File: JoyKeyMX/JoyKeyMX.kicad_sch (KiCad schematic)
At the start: 31 parts, among them J1 DB9_Female, J2 Conn_01x16, J3 Conn_01x02, SW1 SW_WITHLED, SW2 SW_WITHLED, SW4 SW_WITHLED, SW5 SW_WITHLED, SW6 SW_WITHLED, SW7 SW_WITHLED

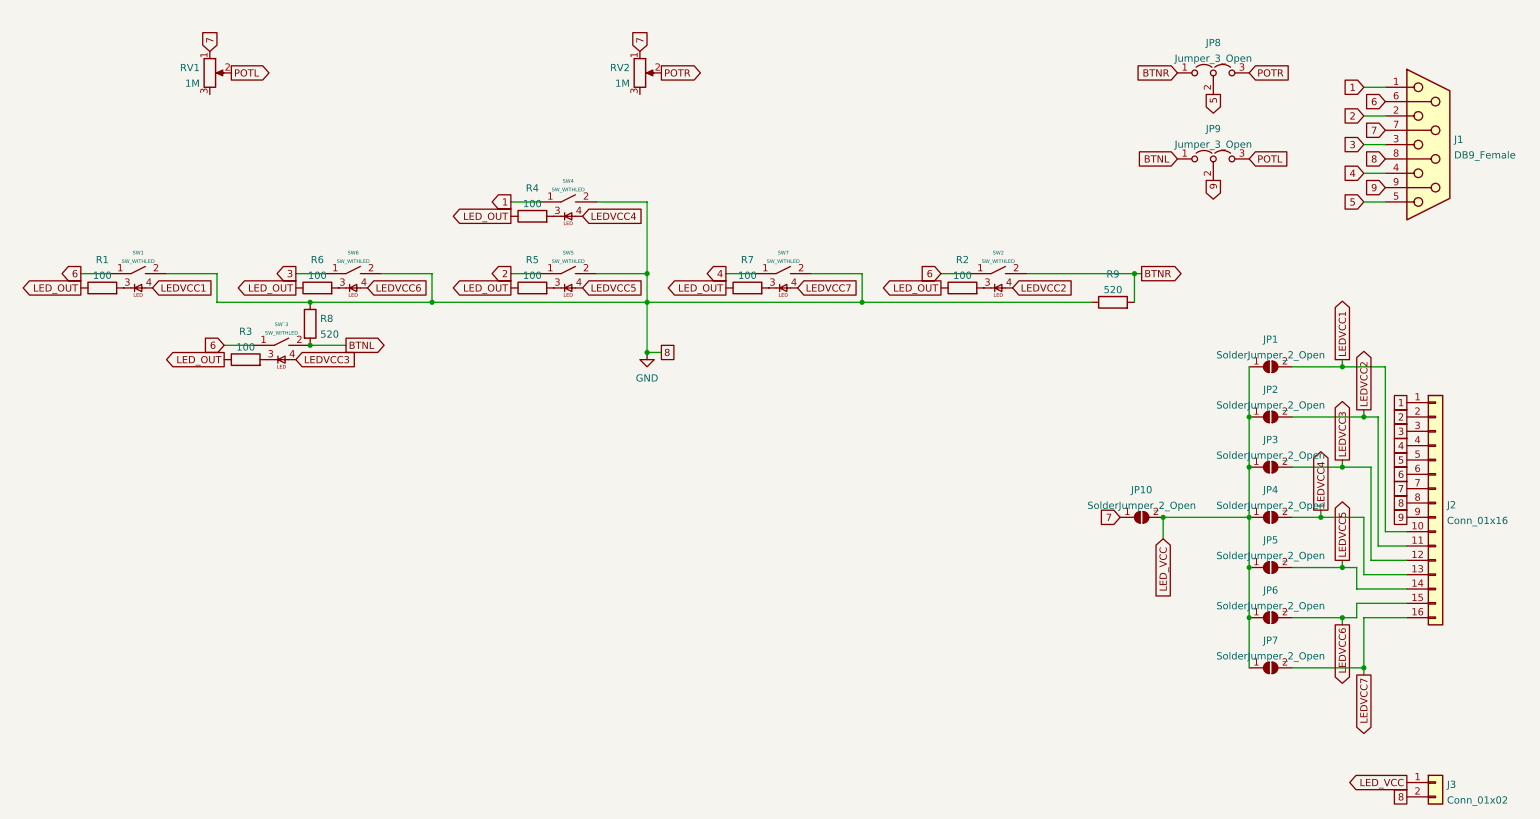
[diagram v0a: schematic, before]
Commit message: Add pins for pots on header
Add branding, fit and finish
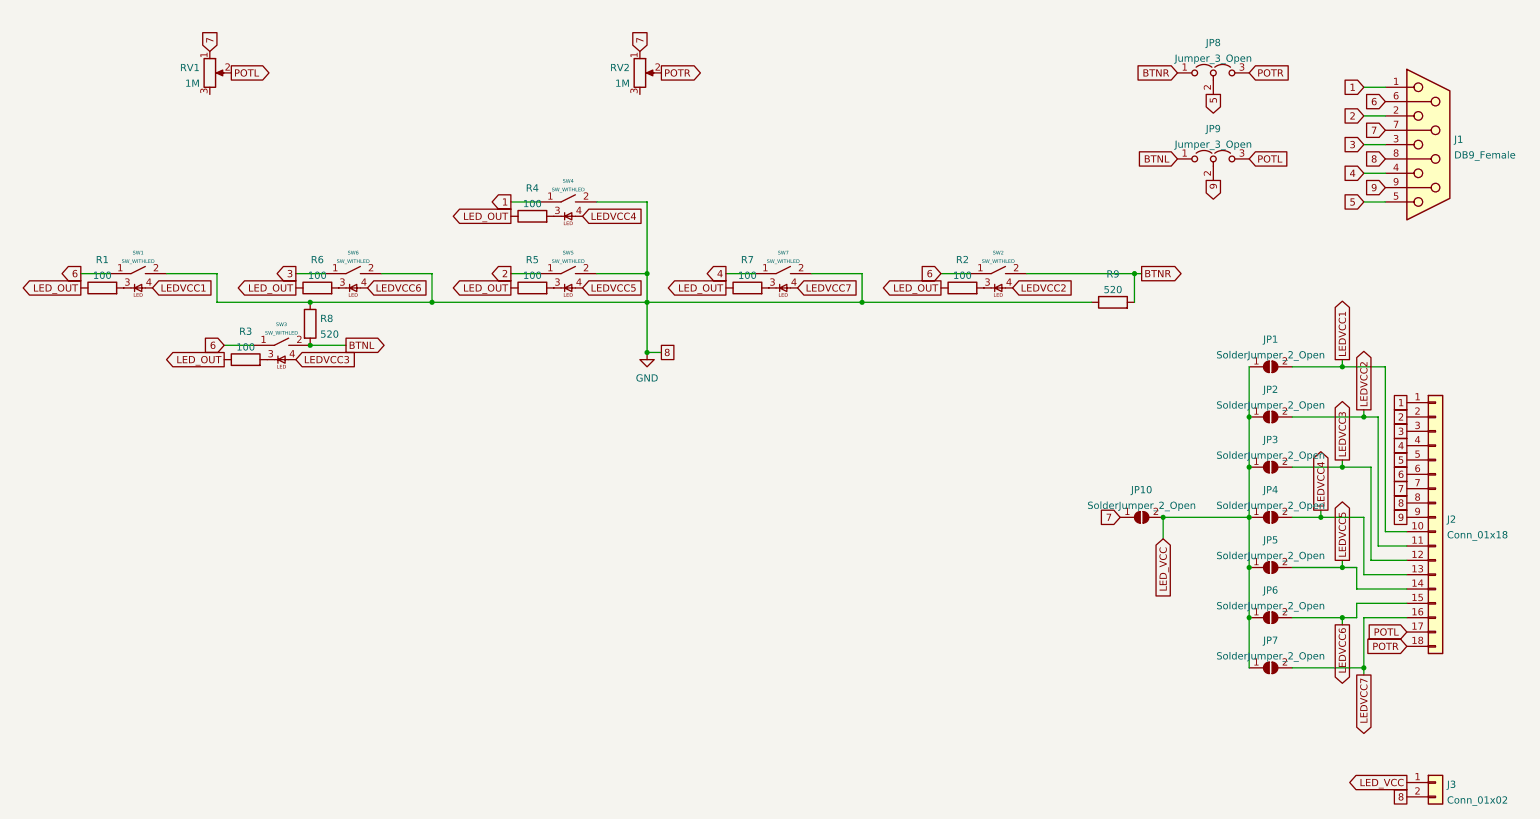
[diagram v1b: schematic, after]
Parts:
- J2: value Conn_01x16 -> Conn_01x18; footprint Connector_PinHeader_2.54mm:PinHeader_1x16_P2.54mm_Vertical -> Connector_PinHeader_2.54mm:PinHeader_1x18_P2.54mm_Vertical; symbol Connector_Generic:Conn_01x16 -> Connector_Generic:Conn_01x18
- renumbered SW`3 to SW3
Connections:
- net POTL: now also J2.17 (Pin_17)
- net POTR: now also J2.18 (Pin_18)
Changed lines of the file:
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@@
     (stroke (width 0) (type default) (color 0 0 0 0))
   )
-  (wire (pts (xy 262.89 109.22) (xy 257.81 109.22))
-    (stroke (width 0) (type default) (color 0 0 0 0))
-  )
-  (wire (pts (xy 262.89 114.3) (xy 255.27 114.3))
+  (wire (pts (xy 255.27 121.92) (xy 262.89 121.92))
     (stroke (width 0) (type default) (color 0 0 0 0))
   )
@@
     (stroke (width 0) (type default) (color 0 0 0 0))
   )
-  (wire (pts (xy 262.89 111.76) (xy 256.54 111.76))
-    (stroke (width 0) (type default) (color 0 0 0 0))
-  )
   (wire (pts (xy 255.27 33.02) (xy 259.08 33.02))
     (stroke (width 0) (type default) (color 0 0 0 0))
@@
     (stroke (width 0) (type default) (color 0 0 0 0))
   )
-  (wire (pts (xy 262.89 116.84) (xy 254 116.84))
-    (stroke (width 0) (type default) (color 0 0 0 0))
-  )
   (wire (pts (xy 142.24 60.96) (xy 147.32 60.96))
     (stroke (width 0) (type default) (color 0 0 0 0))
@@
     (stroke (width 0) (type default) (color 0 0 0 0))
   )
+  (wire (pts (xy 259.08 106.68) (xy 262.89 106.68))
+    (stroke (width 0) (type default) (color 0 0 0 0))
+  )
   (wire (pts (xy 104.14 60.96) (xy 109.22 60.96))
     (stroke (width 0) (type default) (color 0 0 0 0))
@@
     (stroke (width 0) (type default) (color 0 0 0 0))
   )
+  (wire (pts (xy 254 116.84) (xy 262.89 116.84))
+    (stroke (width 0) (type default) (color 0 0 0 0))
+  )
   (wire (pts (xy 215.9 60.96) (xy 214.63 60.96))
     (stroke (width 0) (type default) (color 0 0 0 0))
@@
     (stroke (width 0) (type default) (color 0 0 0 0))
   )
-  (wire (pts (xy 262.89 119.38) (xy 254 119.38))
+  (wire (pts (xy 257.81 109.22) (xy 262.89 109.22))
     (stroke (width 0) (type default) (color 0 0 0 0))
   )
@@
     (stroke (width 0) (type default) (color 0 0 0 0))
   )
+  (wire (pts (xy 256.54 111.76) (xy 262.89 111.76))
+    (stroke (width 0) (type default) (color 0 0 0 0))
+  )
   (wire (pts (xy 255.27 104.14) (xy 247.65 104.14))
     (stroke (width 0) (type default) (color 0 0 0 0))
   )
+  (wire (pts (xy 255.27 130.81) (xy 255.27 121.92))
+    (stroke (width 0) (type default) (color 0 0 0 0))
+  )
   (wire (pts (xy 214.63 60.96) (xy 195.58 60.96))
     (stroke (width 0) (type default) (color 0 0 0 0))
@@
     (stroke (width 0) (type default) (color 0 0 0 0))
   )
-  (wire (pts (xy 262.89 121.92) (xy 255.27 121.92))
+  (wire (pts (xy 255.27 114.3) (xy 262.89 114.3))
     (stroke (width 0) (type default) (color 0 0 0 0))
   )
@@
     (stroke (width 0) (type default) (color 0 0 0 0))
   )
+  (wire (pts (xy 254 119.38) (xy 262.89 119.38))
+    (stroke (width 0) (type default) (color 0 0 0 0))
+  )
   (wire (pts (xy 255.27 130.81) (xy 242.57 130.81))
     (stroke (width 0) (type default) (color 0 0 0 0))
@@
     (stroke (width 0) (type default) (color 0 0 0 0))
   )
-  (wire (pts (xy 262.89 106.68) (xy 259.08 106.68))
-    (stroke (width 0) (type default) (color 0 0 0 0))
-  )
   (wire (pts (xy 247.65 104.14) (xy 242.57 104.14))
     (stroke (width 0) (type default) (color 0 0 0 0))
@@
     (stroke (width 0) (type default) (color 0 0 0 0))
   )
-  (wire (pts (xy 255.27 121.92) (xy 255.27 130.81))
-    (stroke (width 0) (type default) (color 0 0 0 0))
-  )
   (wire (pts (xy 104.14 48.26) (xy 109.22 48.26))
     (stroke (width 0) (type default) (color 0 0 0 0))
@@
     )
   )
+  (global_label "POTL" (shape input) (at 262.89 124.46 180) (fields_autoplaced)
+    (effects (font (size 1.27 1.27)) (justify right))
+    (property "Intersheet References" "${INTERSHEET_REFS}" (id 0) (at 255.8807 124.3806 0)
+      (effects (font (size 1.27 1.27)) (justify right) hide)
+    )
+  )
   (global_label "LEDVCC7" (shape output) (at 255.27 132.08 270) (fields_autoplaced)
     (effects (font (size 1.27 1.27)) (justify right))
@@
     (property "Intersheet References" "${INTERSHEET_REFS}" (id 0) (at 61.6193 25.3206 0)
       (effects (font (size 1.27 1.27)) (justify left) hide)
+    )
+  )
+  (global_label "POTR" (shape input) (at 262.89 127 180) (fields_autoplaced)
+    (effects (font (size 1.27 1.27)) (justify right))
+    (property "Intersheet References" "${INTERSHEET_REFS}" (id 0) (at 255.6388 126.9206 0)
+      (effects (font (size 1.27 1.27)) (justify right) hide)
     )
   )
@@
   (symbol (lib_id "UniversalSwitchWithLED:SW_WITHLED") (at 63.5 73.66 0) (unit 1)
     (in_bom yes) (on_board yes) (fields_autoplaced)
-    (property "Reference" "SW`3" (id 0) (at 63.5 69.9622 0)
+    (property "Reference" "SW3" (id 0) (at 63.5 69.9622 0)
       (effects (font (size 0.635 0.635)))
     )
@@
     (pin "3")
   )
-  (symbol (lib_id "Connector_Generic:Conn_01x16") (at 267.97 101.6 0) (unit 1)
-    (in_bom yes) (on_board yes) (fields_autoplaced)
-    (property "Reference" "J2" (id 0) (at 270.002 101.9615 0)
+  (symbol (lib_id "Connector_Generic:Conn_01x18") (at 267.97 104.14 0) (unit 1)
+    (in_bom yes) (on_board yes) (fields_autoplaced)
+    (property "Reference" "J2" (id 0) (at 270.002 104.5015 0)
       (effects (font (size 1.27 1.27)) (justify left))
     )
-    (property "Value" "Conn_01x16" (id 1) (at 270.002 104.7366 0)
+    (property "Value" "Conn_01x18" (id 1) (at 270.002 107.2766 0)
       (effects (font (size 1.27 1.27)) (justify left))
     )
-    (property "Footprint" "Connector_PinHeader_2.54mm:PinHeader_1x16_P2.54mm_Vertical" (id 2) (at 267.97 101.6 0)
-      (effects (font (size 1.27 1.27)) hide)
-    )
-    (property "Datasheet" "~" (id 3) (at 267.97 101.6 0)
+    (property "Footprint" "Connector_PinHeader_2.54mm:PinHeader_1x18_P2.54mm_Vertical" (id 2) (at 267.97 104.14 0)
+      (effects (font (size 1.27 1.27)) hide)
+    )
+    (property "Datasheet" "~" (id 3) (at 267.97 104.14 0)
       (effects (font (size 1.27 1.27)) hide)
     )
@@
     (pin "15")
     (pin "16")
+    (pin "17")
+    (pin "18")
     (pin "2")
     (pin "3")
@@
     )
     (path "/fe557b0f-d638-42ed-8021-71dd98a76443"
-      (reference "J2") (unit 1) (value "Conn_01x16") (footprint "Connector_PinHeader_2.54mm:PinHeader_1x16_P2.54mm_Vertical")
+      (reference "J2") (unit 1) (value "Conn_01x18") (footprint "Connector_PinHeader_2.54mm:PinHeader_1x18_P2.54mm_Vertical")
     )
     (path "/e702a3ea-106a-406d-9f17-c06eda1e35d1"
@@
       (reference "SW2") (unit 1) (value "SW_WITHLED") (footprint "Universal-Switch-Footprint:MX-ALPs-PG1350-LED-FLIP")
     )
+    (path "/cb2d9bc6-1961-44c0-842e-5cc094e0af1a"
+      (reference "SW3") (unit 1) (value "SW_WITHLED") (footprint "Universal-Switch-Footprint:MX-ALPs-PG1350-LED-FLIP")
+    )
     (path "/5a768132-5548-46f5-9624-91b717ac5a4e"
       (reference "SW4") (unit 1) (value "SW_WITHLED") (footprint "Universal-Switch-Footprint:MX-ALPs-PG1350-LED-FLIP")
@@
       (reference "SW7") (unit 1) (value "SW_WITHLED") (footprint "Universal-Switch-Footprint:MX-ALPs-PG1350-LED-FLIP")
     )
-    (path "/cb2d9bc6-1961-44c0-842e-5cc094e0af1a"
-      (reference "SW`3") (unit 1) (value "SW_WITHLED") (footprint "Universal-Switch-Footprint:MX-ALPs-PG1350-LED-FLIP")
-    )
-  )
+  )

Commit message: JoyKeyMX Rev.B
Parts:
- JP1, JP2, JP3, JP4, JP5, JP6, JP7: footprint Jumper:SolderJumper-2_P1.3mm_Open_TrianglePad1.0x1.5mm -> Jumper:SolderJumper-2_P1.3mm_Bridged_RoundedPad1.0x1.5mm; symbol Jumper:SolderJumper_2_Open -> Jumper:SolderJumper_2_Bridged
- JP8, JP9: footprint Connector_PinHeader_2.54mm:PinHeader_1x03_P2.54mm_Horizontal -> Library:PinHeader_1x03_P2.54mm_Horizontal
- R1, R2, R3, R4, R5, R6, R7, R8, R9: footprint Resistor_THT:R_Axial_DIN0207_L6.3mm_D2.5mm_P7.62mm_Horizontal -> Library:R_Axial_DIN0207_L6.3mm_D2.5mm_P7.62mm_Horizontal (with value on silkscreen)
- RV1, RV2: footprint Potentiometer_THT:Potentiometer_Bourns_PTV09A-1_Single_Vertical -> Library:Potentiometer (centered)
- SW1, SW2, SW3, SW4, SW5, SW6, SW7: footprint Universal-Switch-Footprint:MX-ALPs-PG1350-LED-FLIP -> Library:MX-1U-LED
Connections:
- net LED_OUT is gone; now on net GND: R1.1, R2.1, R3.1, R4.1, R5.1, R6.1, R7.1

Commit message: JoyKey XL PCB and case revision
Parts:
- removed JP1, JP2, JP3, JP4, JP5, JP6, JP7: SolderJumper_2_Open, Jumper:SolderJumper-2_P1.3mm_Bridged_RoundedPad1.0x1.5mm, symbol Jumper:SolderJumper_2_Bridged
- removed JP10: SolderJumper_2_Open, Jumper:SolderJumper-2_P1.3mm_Open_RoundedPad1.0x1.5mm, symbol Jumper:SolderJumper_2_Open
- removed JP9: Jumper_3_Open, Library:PinHeader_1x03_P2.54mm_Horizontal, symbol Jumper:Jumper_3_Open
- added J4: Conn_01x02, Connector_PinHeader_2.54mm:PinHeader_1x02_P2.54mm_Vertical, symbol Connector_Generic:Conn_01x02
- J2: value Conn_01x18 -> Conn_01x09; footprint Connector_PinHeader_2.54mm:PinHeader_1x18_P2.54mm_Vertical -> Connector_PinHeader_2.54mm:PinHeader_1x09_P2.54mm_Vertical; symbol Connector_Generic:Conn_01x18 -> Connector_Generic:Conn_01x09
- JP1: renamed from JP8; value Jumper_3_Open -> DPDT; footprint Library:PinHeader_1x03_P2.54mm_Horizontal -> Button_Switch_THT:SW_CuK_JS202011AQN_DPDT_Angled; symbol Jumper:Jumper_3_Open -> Switch:SW_Push_DPDT
- R1, R2, R3, R4, R5, R6, R7, R8, R9: footprint Library:R_Axial_DIN0207_L6.3mm_D2.5mm_P7.62mm_Horizontal (with value on silkscreen) -> Resistor_SMD:R_0603_1608Metric
- SW1, SW2, SW3, SW4, SW5, SW6, SW7: footprint Library:MX-1U-LED -> Library:MX-1-00U-LED
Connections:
- net LED_VCC is gone; now on net 7: J3.1 (Pin_1)
- net 9: now also JP1.5 (B)
- net BTNL: now also JP1.4 (A)
- net POTL: now also JP1.6 (C), J4.1 (Pin_1); no longer J2.17 (Pin_17)
- net POTR: now also J4.2 (Pin_2); no longer J2.18 (Pin_18)
- net LEDVCC1 renamed LEDVCC
- net LEDVCC: now also SW2.4, SW3.4, SW4.4, SW5.4, SW6.4, SW7.4; no longer J2.10 (Pin_10)
- removed net LEDVCC2: J2.11 (Pin_11), SW2.4
- removed net LEDVCC3: J2.12 (Pin_12), SW3.4
- removed net LEDVCC4: J2.13 (Pin_13), SW4.4
- removed net LEDVCC5: J2.14 (Pin_14), SW5.4
- removed net LEDVCC6: J2.15 (Pin_15), SW6.4
- removed net LEDVCC7: J2.16 (Pin_16), SW7.4
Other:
- moved on the sheet: J1, J3

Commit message: Fix JoyKey XL backlight connection
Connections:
- net LEDVCC is gone; now on net 7: SW1.4, SW2.4, SW3.4, SW4.4, SW5.4, SW6.4, SW7.4
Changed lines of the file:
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@@
+    (stroke (width 0) (type default))
+  )
+  (wire (pts (xy 224.79 46.99) (xy 228.6 46.99))
     (stroke (width 0) (type default))
   )
@@
     )
   )
-  (global_label "LEDVCC" (shape input) (at 154.94 63.5 0) (fields_autoplaced)
-    (effects (font (size 1.27 1.27)) (justify left))
-    (property "Intersheetrefs" "${INTERSHEET_REFS}" (at 164.9215 63.5 0)
+  (global_label "LED_VCC" (shape input) (at 154.94 63.5 0) (fields_autoplaced)
+    (effects (font (size 1.27 1.27)) (justify left))
+    (property "Intersheetrefs" "${INTERSHEET_REFS}" (at 165.8891 63.5 0)
       (effects (font (size 1.27 1.27)) (justify left) hide)
     )
@@
     )
   )
-  (global_label "7" (shape input) (at 228.6 46.99 180) (fields_autoplaced)
-    (effects (font (size 1.27 1.27)) (justify right))
-    (property "Intersheetrefs" "${INTERSHEET_REFS}" (at 224.9774 46.9106 0)
+  (global_label "7" (shape input) (at 224.79 46.99 180) (fields_autoplaced)
+    (effects (font (size 1.27 1.27)) (justify right))
+    (property "Intersheetrefs" "${INTERSHEET_REFS}" (at 221.1674 46.9106 0)
       (effects (font (size 1.27 1.27)) (justify right) hide)
     )
@@
     )
   )
-  (global_label "LEDVCC" (shape input) (at 66.04 76.2 0) (fields_autoplaced)
-    (effects (font (size 1.27 1.27)) (justify left))
-    (property "Intersheetrefs" "${INTERSHEET_REFS}" (at 76.0215 76.2 0)
+  (global_label "LED_VCC" (shape input) (at 66.04 76.2 0) (fields_autoplaced)
+    (effects (font (size 1.27 1.27)) (justify left))
+    (property "Intersheetrefs" "${INTERSHEET_REFS}" (at 76.9891 76.2 0)
       (effects (font (size 1.27 1.27)) (justify left) hide)
     )
@@
     )
   )
-  (global_label "LEDVCC" (shape input) (at 78.74 63.5 0) (fields_autoplaced)
-    (effects (font (size 1.27 1.27)) (justify left))
-    (property "Intersheetrefs" "${INTERSHEET_REFS}" (at 88.7215 63.5 0)
+  (global_label "LED_VCC" (shape input) (at 78.74 63.5 0) (fields_autoplaced)
+    (effects (font (size 1.27 1.27)) (justify left))
+    (property "Intersheetrefs" "${INTERSHEET_REFS}" (at 89.6891 63.5 0)
       (effects (font (size 1.27 1.27)) (justify left) hide)
     )
@@
     )
   )
-  (global_label "LEDVCC" (shape input) (at 116.84 50.8 0) (fields_autoplaced)
-    (effects (font (size 1.27 1.27)) (justify left))
-    (property "Intersheetrefs" "${INTERSHEET_REFS}" (at 126.8215 50.8 0)
+  (global_label "LED_VCC" (shape input) (at 116.84 50.8 0) (fields_autoplaced)
+    (effects (font (size 1.27 1.27)) (justify left))
+    (property "Intersheetrefs" "${INTERSHEET_REFS}" (at 127.7891 50.8 0)
       (effects (font (size 1.27 1.27)) (justify left) hide)
     )
@@
     )
   )
-  (global_label "LEDVCC" (shape input) (at 116.84 63.5 0) (fields_autoplaced)
-    (effects (font (size 1.27 1.27)) (justify left))
-    (property "Intersheetrefs" "${INTERSHEET_REFS}" (at 126.8215 63.5 0)
-      (effects (font (size 1.27 1.27)) (justify left) hide)
-    )
-  )
-  (global_label "LEDVCC" (shape input) (at 193.04 63.5 0) (fields_autoplaced)
-    (effects (font (size 1.27 1.27)) (justify left))
-    (property "Intersheetrefs" "${INTERSHEET_REFS}" (at 203.0215 63.5 0)
-      (effects (font (size 1.27 1.27)) (justify left) hide)
-    )
-  )
-  (global_label "LEDVCC" (shape input) (at 40.64 63.5 0) (fields_autoplaced)
-    (effects (font (size 1.27 1.27)) (justify left))
-    (property "Intersheetrefs" "${INTERSHEET_REFS}" (at 50.6215 63.5 0)
-      (effects (font (size 1.27 1.27)) (justify left) hide)
-    )
+  (global_label "LED_VCC" (shape input) (at 116.84 63.5 0) (fields_autoplaced)
+    (effects (font (size 1.27 1.27)) (justify left))
+    (property "Intersheetrefs" "${INTERSHEET_REFS}" (at 127.7891 63.5 0)
+      (effects (font (size 1.27 1.27)) (justify left) hide)
+    )
+  )
+  (global_label "LED_VCC" (shape input) (at 193.04 63.5 0) (fields_autoplaced)
+    (effects (font (size 1.27 1.27)) (justify left))
+    (property "Intersheetrefs" "${INTERSHEET_REFS}" (at 203.9891 63.5 0)
+      (effects (font (size 1.27 1.27)) (justify left) hide)
+    )
+  )
+  (global_label "LED_VCC" (shape input) (at 40.64 63.5 0) (fields_autoplaced)
+    (effects (font (size 1.27 1.27)) (justify left))
+    (property "Intersheetrefs" "${INTERSHEET_REFS}" (at 51.5891 63.5 0)
+      (effects (font (size 1.27 1.27)) (justify left) hide)
+    )
